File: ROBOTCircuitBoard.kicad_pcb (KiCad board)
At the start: 2 copper layers, 60.5 x 76.5 mm, 18 parts, among them J1 DB15_HighDensity_MountingHoles, J2 DB15_HighDensity_MountingHoles, P1 CONN_01X03, P13 CONN_01X04, P15 CONN_01X04, P2 CONN_01X04, P24 CONN_01X04, P3 CONN_01X04, P4 CONN_01X04, P5 CONN_01X05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

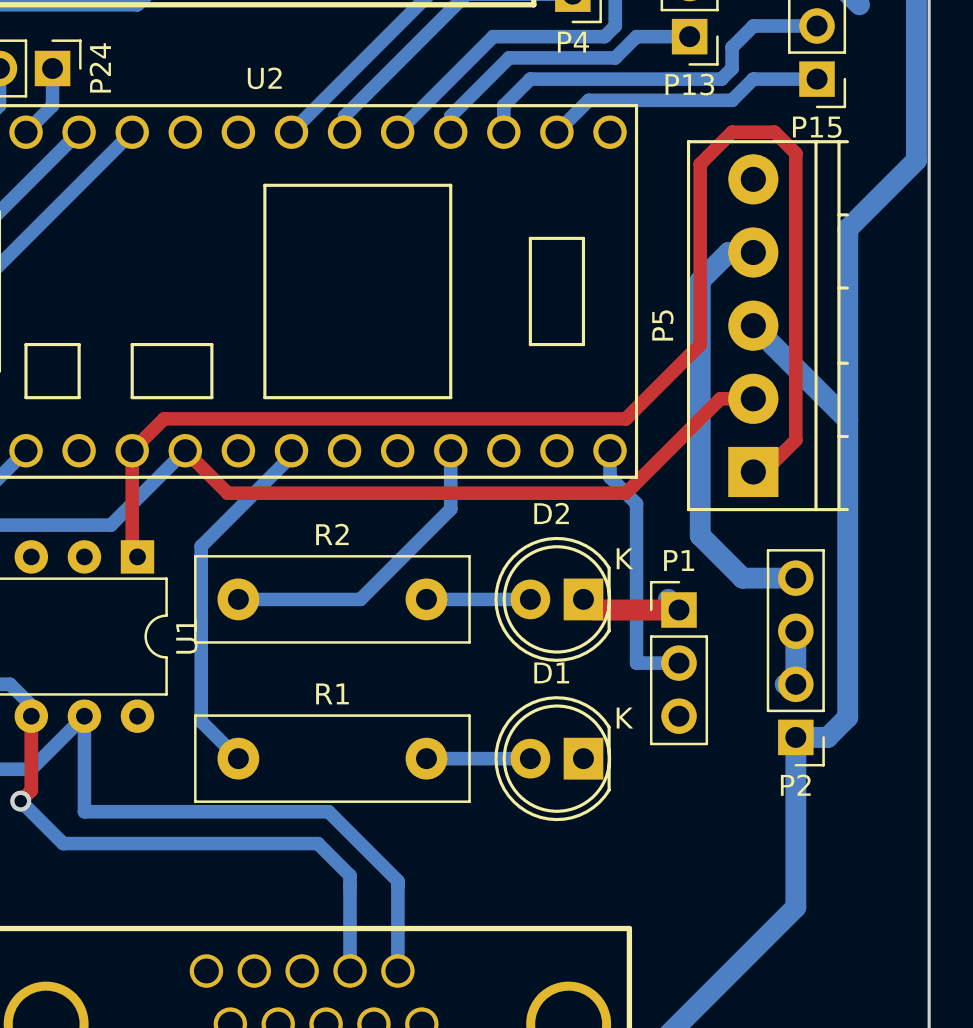
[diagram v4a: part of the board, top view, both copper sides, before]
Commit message: changed footprints and updated part number
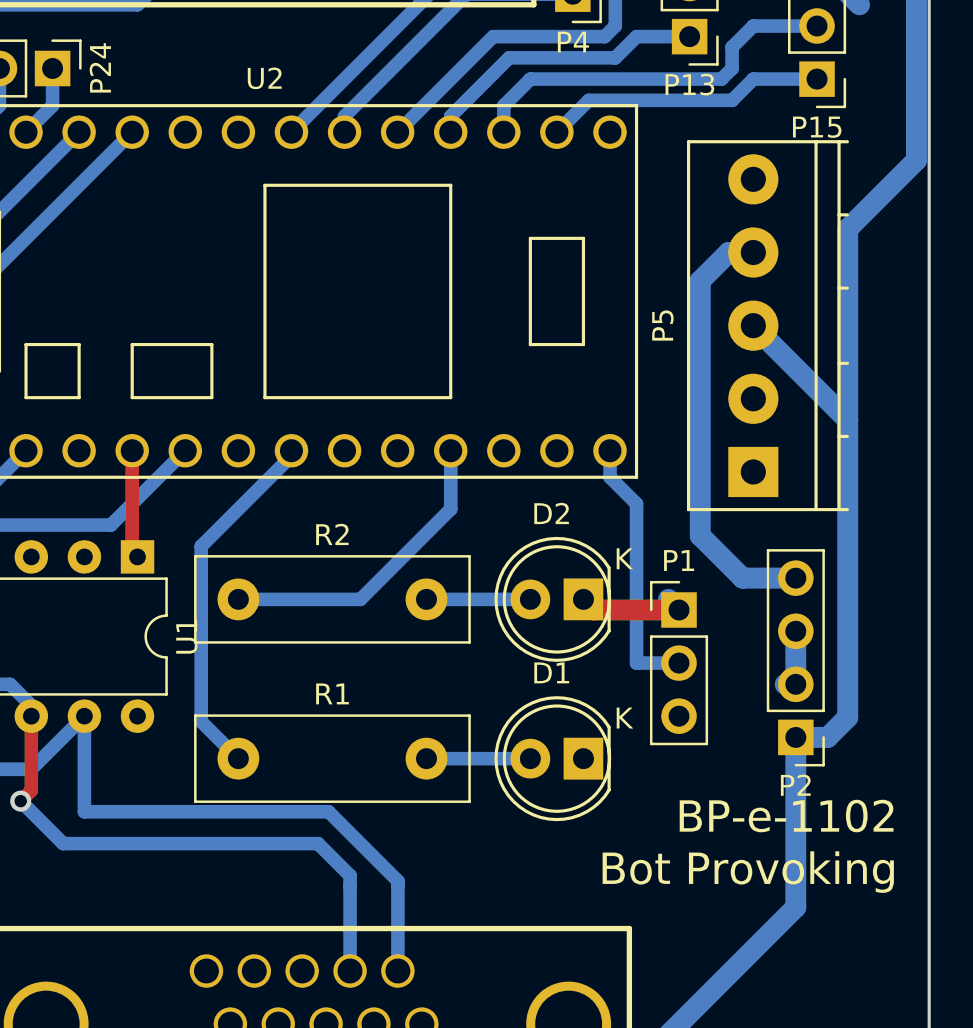
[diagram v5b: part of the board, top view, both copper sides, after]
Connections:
- J1 pad 11: Net-(J1-Pad11) -> (no net)
- J1 pad 3: Net-(J1-Pad3) -> (no net)
- J1 pad 4: Net-(J1-Pad4) -> (no net)
- J1 pad 5: Net-(J1-Pad5) -> (no net)
- J2 pad 11: Net-(J2-Pad11) -> (no net)
- J2 pad 3: Net-(J2-Pad3) -> (no net)
- J2 pad 4: Net-(J2-Pad4) -> (no net)
- J2 pad 5: Net-(J2-Pad5) -> (no net)
- P13 pad 3: GND -> +5V
- P13 pad 4: +5V -> GND
- P15 pad 3: GND -> +5V
- P15 pad 4: +5V -> GND
- P24 pad 3: GND -> +5V
- P24 pad 4: +5V -> GND
- P3 pad 3: GND -> +5V
- P3 pad 4: +5V -> GND
- P4 pad 3: GND -> +5V
- P4 pad 4: +5V -> GND
- P5 pad 1: /CAN_Tx -> /CANL
- P5 pad 2: /CAN_Rx -> /CANH
- P6 pad 3: GND -> +5V
- P6 pad 4: +5V -> GND
- U1 pad 5: Net-(U1-Pad5) -> (no net)
- U2 pad 10: Net-(U2-Pad10) -> (no net)
- U2 pad 12: Net-(U2-Pad12) -> (no net)
- U2 pad 13: Net-(U2-Pad13) -> (no net)
- U2 pad 20: Net-(U2-Pad20) -> (no net)
- U2 pad 27: /A4 -> (no net)
- U2 pad 28: /A5 -> (no net)
- U2 pad 4: Net-(U2-Pad4) -> (no net)
- U2 pad 7: Net-(U2-Pad7) -> (no net)
- U2 pad 9: Net-(U2-Pad9) -> (no net)
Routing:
- net /CAN_Tx: track 65.1 -> 5.19 mm
- net /CAN_Rx: track 42.5 -> 12.6 mm
- net GND: track 20.9 -> 11.7 mm
- net +5V: track 22.1 -> 31.3 mm
- net /CANL: track 103.1 -> 103.7 mm
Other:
- board text added: "BP-e-1102"
- board text removed: "BP 0203"

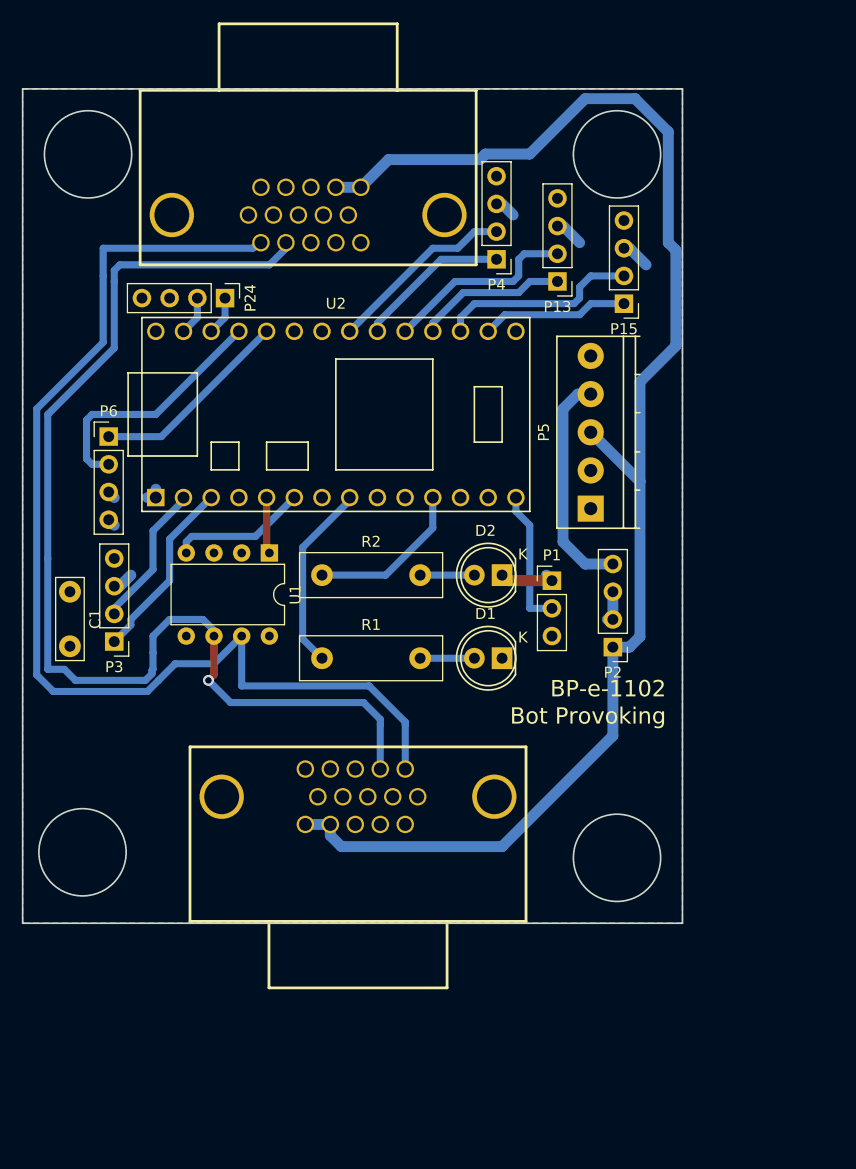
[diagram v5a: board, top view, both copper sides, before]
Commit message: Redid filled areas and labeled the 3-4 pin connecters and pololu port. Note: Silkscreen orientation will be looked into further.
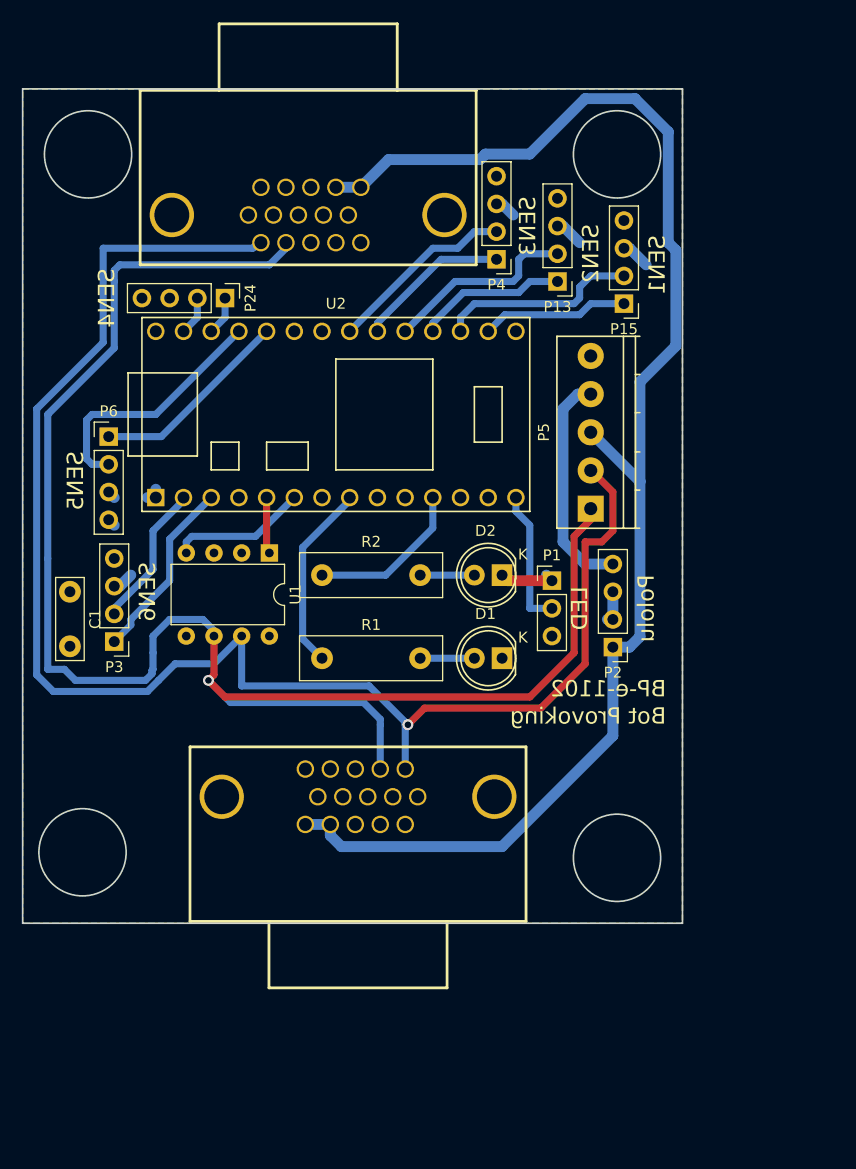
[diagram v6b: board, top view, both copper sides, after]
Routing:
- net /CANL: track 103.7 -> 152.8 mm
- net /CANH: track 103.4 -> 142.7 mm, vias 0 -> 1
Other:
- board text added: "LED"
- board text added: "Pololu"
- board text added: "SEN1"
- board text added: "SEN2"
- board text added: "SEN3"
- board text added: "SEN4"
- board text added: "SEN5"
- board text added: "SEN6"
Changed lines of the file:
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@@
   (general
     (links 72)
-    (no_connects 16)
-    (area 143.924999 87.424999 204.575001 164.075001)
+    (no_connects 2)
+    (area 143.924999 81.206999 204.592004 170.253001)
     (thickness 1.6)
-    (drawings 12)
-    (tracks 170)
+    (drawings 20)
+    (tracks 186)
     (zones 0)
     (modules 18)
@@
     )
   )
+  (gr_text LED (at 195.072 135.128 90) (layer F.SilkS)
+    (effects (font (size 1.5 1.5) (thickness 0.3)) (justify mirror))
+  )
+  (gr_text "SEN6\n" (at 155.448 133.604 90) (layer F.SilkS)
+    (effects (font (size 1.5 1.5) (thickness 0.3)) (justify mirror))
+  )
+  (gr_text SEN5 (at 148.844 123.444 90) (layer F.SilkS)
+    (effects (font (size 1.5 1.5) (thickness 0.3)) (justify mirror))
+  )
+  (gr_text "SEN4\n\n" (at 152.908 106.68 90) (layer F.SilkS)
+    (effects (font (size 1.5 1.5) (thickness 0.3)) (justify mirror))
+  )
+  (gr_text "SEN3\n\n" (at 191.516 100.076 90) (layer F.SilkS)
+    (effects (font (size 1.5 1.5) (thickness 0.3)) (justify mirror))
+  )
+  (gr_text "SEN2\n" (at 196.088 102.616 90) (layer F.SilkS)
+    (effects (font (size 1.5 1.5) (thickness 0.3)) (justify mirror))
+  )
+  (gr_text SEN1 (at 202.184 103.632 90) (layer F.SilkS)
+    (effects (font (size 1.5 1.5) (thickness 0.3)) (justify mirror))
+  )
+  (gr_text Pololu (at 201.168 135.128 90) (layer F.SilkS)
+    (effects (font (size 1.5 1.5) (thickness 0.3)) (justify mirror))
+  )
   (gr_text "Bot Provoking" (at 203 145) (layer F.SilkS)
-    (effects (font (size 1.5 1.5) (thickness 0.3)) (justify right))
+    (effects (font (size 1.5 1.5) (thickness 0.3)) (justify left mirror))
   )
   (gr_text BP-e-1102 (at 203 142.5) (layer F.SilkS)
-    (effects (font (size 1.5 1.5) (thickness 0.3)) (justify right))
+    (effects (font (size 1.5 1.5) (thickness 0.3)) (justify left mirror))
   )
   (gr_text "Bot Provoking" (at 146 149) (layer B.SilkS)
-    (effects (font (size 1.5 1.5) (thickness 0.3)) (justify right mirror))
+    (effects (font (size 1.5 1.5) (thickness 0.3)) (justify left))
   )
   (gr_text BP-e-1102 (at 146 146.5) (layer B.SilkS)
-    (effects (font (size 1.5 1.5) (thickness 0.3)) (justify right mirror))
+    (effects (font (size 1.5 1.5) (thickness 0.3)) (justify left))
   )
   (gr_line (start 144 87.5) (end 144 164) (angle 90) (layer Edge.Cuts) (width 0.15))
@@
   (segment (start 196.088 115.484) (end 195.92 115.484) (width 1) (layer B.Cu) (net 6))
   (segment (start 148.844 133.604) (end 148.336 133.604) (width 1) (layer B.Cu) (net 6))
+  (segment (start 196.088 122.484) (end 196.144 122.484) (width 0.65) (layer F.Cu) (net 7) (status C00000))
+  (segment (start 196.144 122.484) (end 198.12 124.46) (width 0.65) (layer F.Cu) (net 7) (status 400000))
+  (segment (start 198.12 124.46) (end 198.12 128.016) (width 0.65) (layer F.Cu) (net 7))
+  (segment (start 198.12 128.016) (end 197.104 129.032) (width 0.65) (layer F.Cu) (net 7))
+  (segment (start 197.104 129.032) (end 195.58 129.032) (width 0.65) (layer F.Cu) (net 7))
+  (segment (start 195.58 129.032) (end 195.58 140.208) (width 0.65) (layer F.Cu) (net 7))
+  (segment (start 195.58 140.208) (end 191.516 144.272) (width 0.65) (layer F.Cu) (net 7))
+  (segment (start 191.516 144.272) (end 180.848 144.272) (width 0.65) (layer F.Cu) (net 7))
+  (segment (start 180.848 144.272) (end 179.324 145.796) (width 0.65) (layer F.Cu) (net 7))
+  (via (at 179.324 145.796) (size 1) (drill 0.6) (layers F.Cu B.Cu) (net 7))
+  (segment (start 179.324 145.796) (end 179.082 145.796) (width 0.65) (layer B.Cu) (net 7))
   (segment (start 179.082 149.86) (end 179.082 145.796) (width 0.65) (layer B.Cu) (net 7))
   (segment (start 164.084 142.24) (end 164.084 137.668) (width 0.65) (layer B.Cu) (net 7))
@@
   (segment (start 165.608 101.6) (end 165.85 101.6) (width 0.65) (layer B.Cu) (net 7))
   (segment (start 165.85 101.6) (end 165.85 101.866) (width 0.65) (layer B.Cu) (net 7))
+  (segment (start 196.088 125.984) (end 196.088 127) (width 0.65) (layer F.Cu) (net 8) (status C00000))
+  (segment (start 196.088 127) (end 194.564 128.524) (width 0.65) (layer F.Cu) (net 8) (status 400000))
+  (segment (start 194.564 128.524) (end 194.564 139.192) (width 0.65) (layer F.Cu) (net 8))
+  (segment (start 194.564 139.192) (end 190.5 143.256) (width 0.65) (layer F.Cu) (net 8))
+  (segment (start 190.5 143.256) (end 162.56 143.256) (width 0.65) (layer F.Cu) (net 8))
+  (segment (start 162.56 143.256) (end 161.036 141.732) (width 0.65) (layer F.Cu) (net 8))
   (segment (start 176.792 149.86) (end 176.792 145.796) (width 0.65) (layer B.Cu) (net 8))
   (segment (start 161.544 141.224) (end 161.544 137.668) (width 0.65) (layer F.Cu) (net 8))
@@
   (segment (start 154.94 141.732) (end 155.261916 141.732) (width 0.65) (layer B.Cu) (net 8))
   (segment (start 161.544 137.16) (end 161.544 137.668) (width 0.65) (layer B.Cu) (net 8))
-  (segment (start 196.088 125.984) (end 196.596 125.984) (width 0.65) (layer F.Cu) (net 8))
   (segment (start 192.532 135.128) (end 190.5 135.128) (width 0.65) (layer B.Cu) (net 10))
   (segment (start 189.23 126.238) (end 189.23 124.968) (width 0.65) (layer B.Cu) (net 10))
